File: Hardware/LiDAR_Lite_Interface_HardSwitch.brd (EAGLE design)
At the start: 50.2 x 56.2 mm, 40 parts, among them J1 CONN_6SCREW_2.54, J2 CONN_42.54_SCREW, Q1 2N7002, Q2 2N7002, Q3 DMG3404, Q4 MOSFET_PCH-NX2301P, U1 TLV61220DBV, U2 TCS40DPRSOT23, U4 LIS3DHLGA, U5 MIC53653.3SC70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

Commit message: Design updates and gerbers, final DFM required
Added Gerbers for OSH park, naming update, pending v0.2 design
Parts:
- removed Q4: MOSFET_PCH-NX2301P, bschulz:SOT23-3
- added C13: (no value), bschulz_passives:C0603
- added J3: (no value), bschulz:1X02
- added JP1: JUMPER-SMT_2_NC_PASTE_SILK, SparkFun-Jumpers:SMT-JUMPER_2_NC_PASTE_SILK
- added R12: 2.2k, bschulz_passives:R0603
- added R13: 1.8k, bschulz_passives:R0603
- added R14: 10k, bschulz_passives:R0603
- added U7: MIC2544MSOP, bschulz:MSOP_8
- Q1, Q2: value 2N7002 -> MOSFET-NCH-2N7002P
- moved C1 3.81 mm to (18.3, 5.33)
- moved R9 1.27 mm to (14.2, 54.0), turned to 180 degrees
- moved ISP1 0.90 mm to (13.6, 49.0), turned to 180 degrees
- moved L1 0.89 mm to (37.7, 11.4)
- moved U1 0.89 mm to (32.6, 11.4)
- moved C4 0.89 mm to (29.8, 12.4)
- moved R7 0.89 mm to (29.7, 8.76)
- moved R8 0.89 mm to (32.4, 8.26)
- moved C3 0.89 mm to (35.3, 10.7)
- moved R1 0.51 mm to (16.5, 42.7)
- moved R11 0.51 mm to (14.0, 42.7)
- moved R2 0.51 mm to (19.1, 42.7)
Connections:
- new net FAULT: R14.1, U3.4, U7.2
- new net N$5: JP1.1, R12.2, U7.5
- new net N$6: JP1.2, R13.2
- net 5V: now also C13.1, R14.2, U7.7; no longer Q4.2
- net 5V_SW: now also U7.6, U7.8; no longer Q4.3
- net GND: now also C13.2, J3.1, R12.1, R13.1, U7.3
- net N$4: now also J3.2
- net POWER_SW: now also U7.1; no longer Q4.1
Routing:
- net FAULT: track 0.00 -> 57.9 mm, vias 0 -> 5
- net GND: track 200.2 -> 214.3 mm, vias 10 -> 12
- net 5V: track 140.0 -> 152.3 mm
- net 5V_SW: track 37.2 -> 45.9 mm
- net SCL: track 44.7 -> 37.0 mm
- net MISO: track 23.8 -> 18.4 mm
- net !RESET: track 20.9 -> 15.9 mm
- net N$5: track 0.00 -> 4.52 mm
- net POWER_SW: track 51.5 -> 54.9 mm
- net N$4: track 1.93 -> 4.10 mm
- net N$6: track 0.00 -> 2.07 mm
- net SDA: track 51.7 -> 50.8 mm
- net SCL_OB: track 41.3 -> 40.6 mm
- added copper zone on layer 1, net 5V_SW
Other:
- board text added: "+"
- board text added: "-"
- board text added: "Project-Symbiont-LiDAR v0.1.0 07-12-2019 Bobby Schulz Northern Widget LLC and University of Minnesota"
- board text added: "STAT"
- board text removed: "Project-Symbiont-LiDAR v0.0.0 07-12-2019 Bobby Schulz Northern Widget LLC and University of Minnesota"

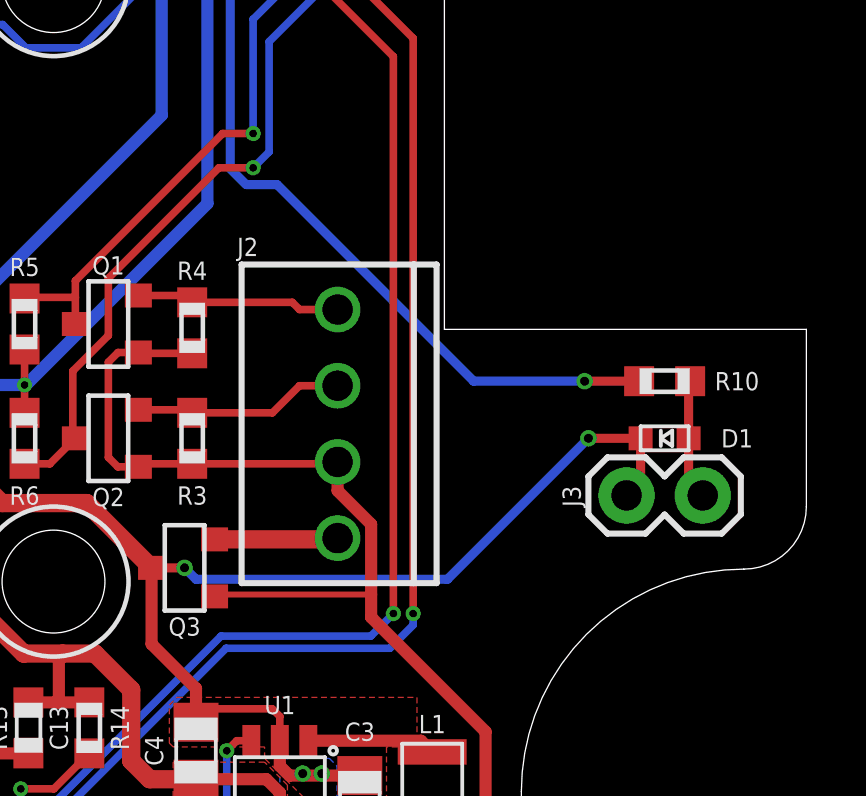
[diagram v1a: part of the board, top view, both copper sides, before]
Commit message: Minor edits, changed external LED topology, sent v0.1 to fab
Changed external LED to use independent resistor, generated gerbers, sent v0.1 to fab
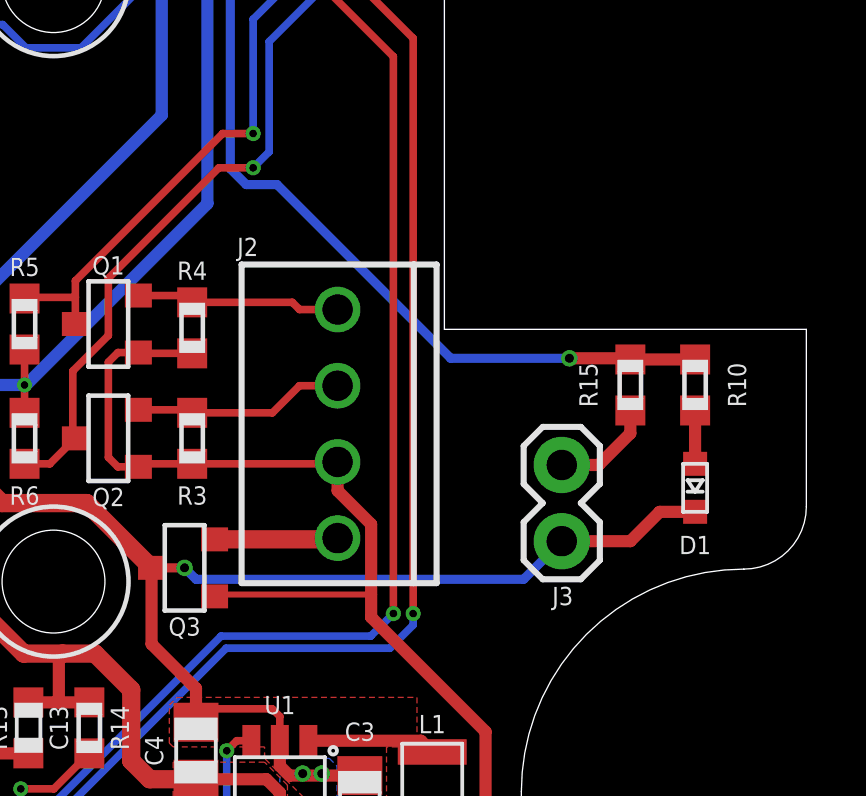
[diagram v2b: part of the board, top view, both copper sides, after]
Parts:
- added R15: 330, bschulz_passives:R0603
- moved J3 2.64 mm to (42.0, 19.4), turned to 90 degrees
- moved D1 1.94 mm to (46.5, 21.2), turned to 90 degrees
- moved R10 1.02 mm to (46.5, 24.6), turned to 90 degrees
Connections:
- new net N$2: D1.ANODE, R10.1
- net N$4: now also R15.1; no longer D1.ANODE, R10.1
- net STAT_LED: now also R15.2
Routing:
- net N$2: track 0.00 -> 1.78 mm
- net STAT_LED: track 34.4 -> 36.0 mm
- net GND: track 214.3 -> 213.0 mm, vias 12 -> 11
- net N$4: track 4.10 -> 3.48 mm
